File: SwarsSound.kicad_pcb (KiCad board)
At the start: 2 copper layers, 292.1 x 227.3 mm, 168 parts, among them P1 Main_Connector, P2 aud_con, P3 edge_con, Q1 2N3906f, Q2 2N3906f, Q3 2N3904, Q4 2N3904

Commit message: more traces
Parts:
- moved R27 2.62 mm to (117.5, 111.1), turned to 270 degrees
- moved C28 1.27 mm to (132.1, 172.7), turned to 0 degrees
- turned R26 to 0 degrees
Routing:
- net SPEECH: track 3.81 -> 171.4 mm
- net Net-(D-2-Pad24): track 0.00 -> 123.0 mm, vias 0 -> 1
- net +5A: track 0.00 -> 73.2 mm
- net Net-(C40-Pad1): track 0.00 -> 41.3 mm
- net CO3: track 28.4 -> 0.00 mm
- net CO2: track 14.6 -> 33.6 mm
- net Net-(C38-Pad1): track 0.00 -> 14.5 mm
- net Net-(C-4-Pad7): track 0.00 -> 11.0 mm
- net Net-(C42-Pad1): track 0.00 -> 10.8 mm
- net Net-(C56-Pad1): track 5.08 -> 9.12 mm

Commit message: more traces
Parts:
- moved R8 1.27 mm to (132.7, 35.6), turned to 90 degrees
- moved R9 1.27 mm to (132.7, 38.1), turned to 90 degrees
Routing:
- net SD4: track 266.2 -> 334.3 mm, vias 3 -> 4
- net SD3: track 271.8 -> 339.8 mm, vias 2 -> 3
- net SD6: track 283.9 -> 349.2 mm, vias 3 -> 4
- net SD5: track 277.1 -> 342.0 mm, vias 3 -> 5
- net SD2: track 260.9 -> 319.4 mm, vias 3 -> 4
- net SD7: track 287.2 -> 340.8 mm, vias 3 -> 5
- net SD1: track 257.0 -> 310.5 mm, vias 4 -> 5
- net SA0: track 289.8 -> 342.4 mm, vias 2 -> 4
- net SD0: track 253.4 -> 301.5 mm, vias 2 -> 3
- net DXMT: track 0.00 -> 43.1 mm
- net SA2: track 286.3 -> 327.0 mm, vias 3 -> 5
- net DRCV: track 0.00 -> 38.3 mm
- net CO3: track 0.00 -> 28.7 mm
- net SA5: track 261.7 -> 287.6 mm
- net SA1: track 289.2 -> 307.8 mm, vias 2 -> 3

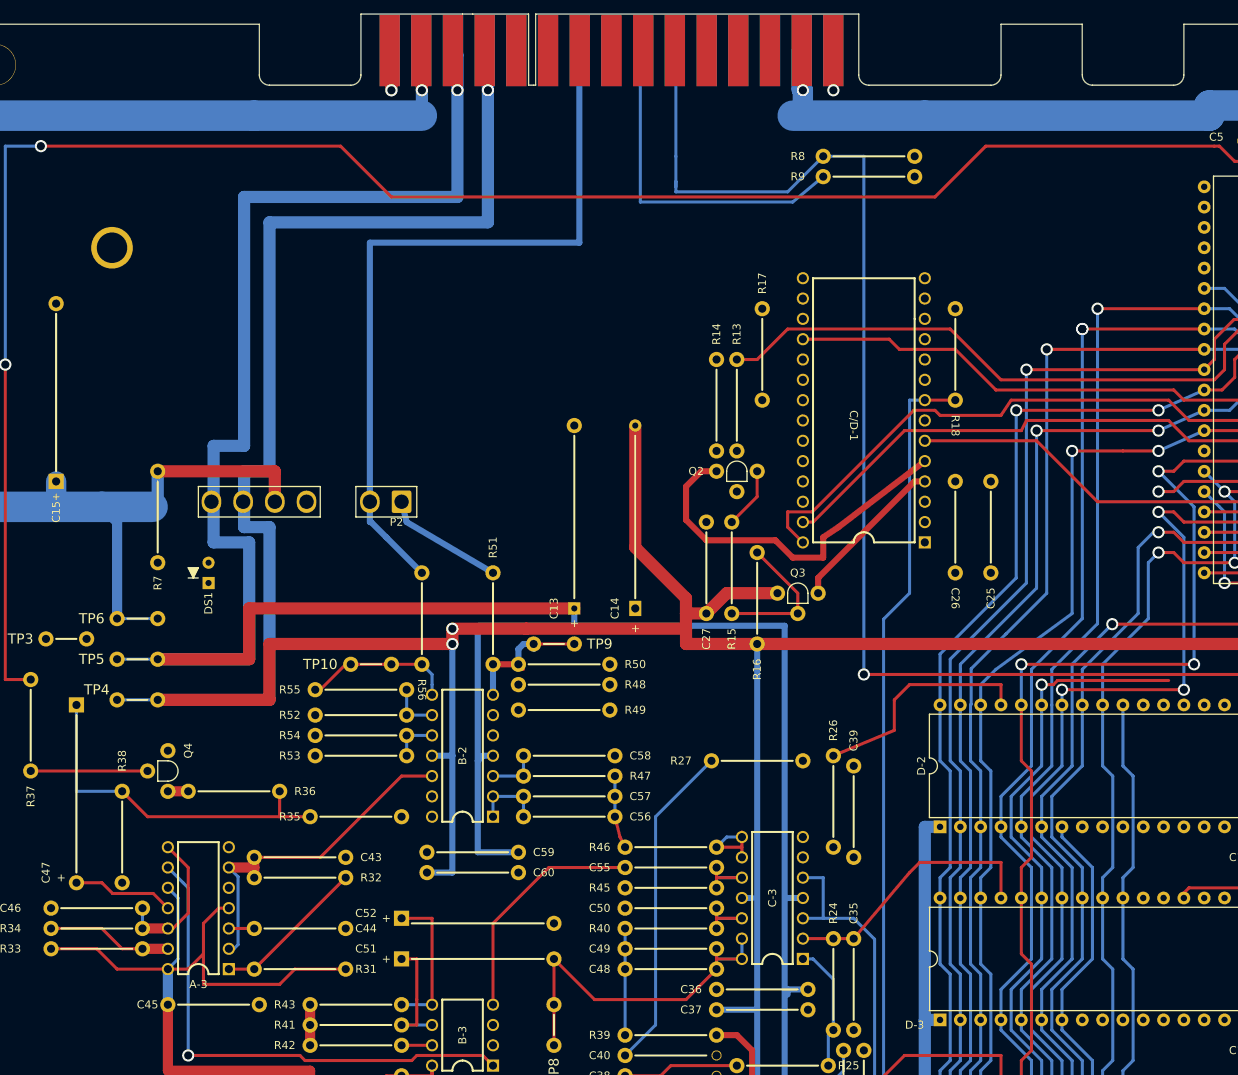
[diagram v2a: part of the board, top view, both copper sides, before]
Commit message: Modified some traces
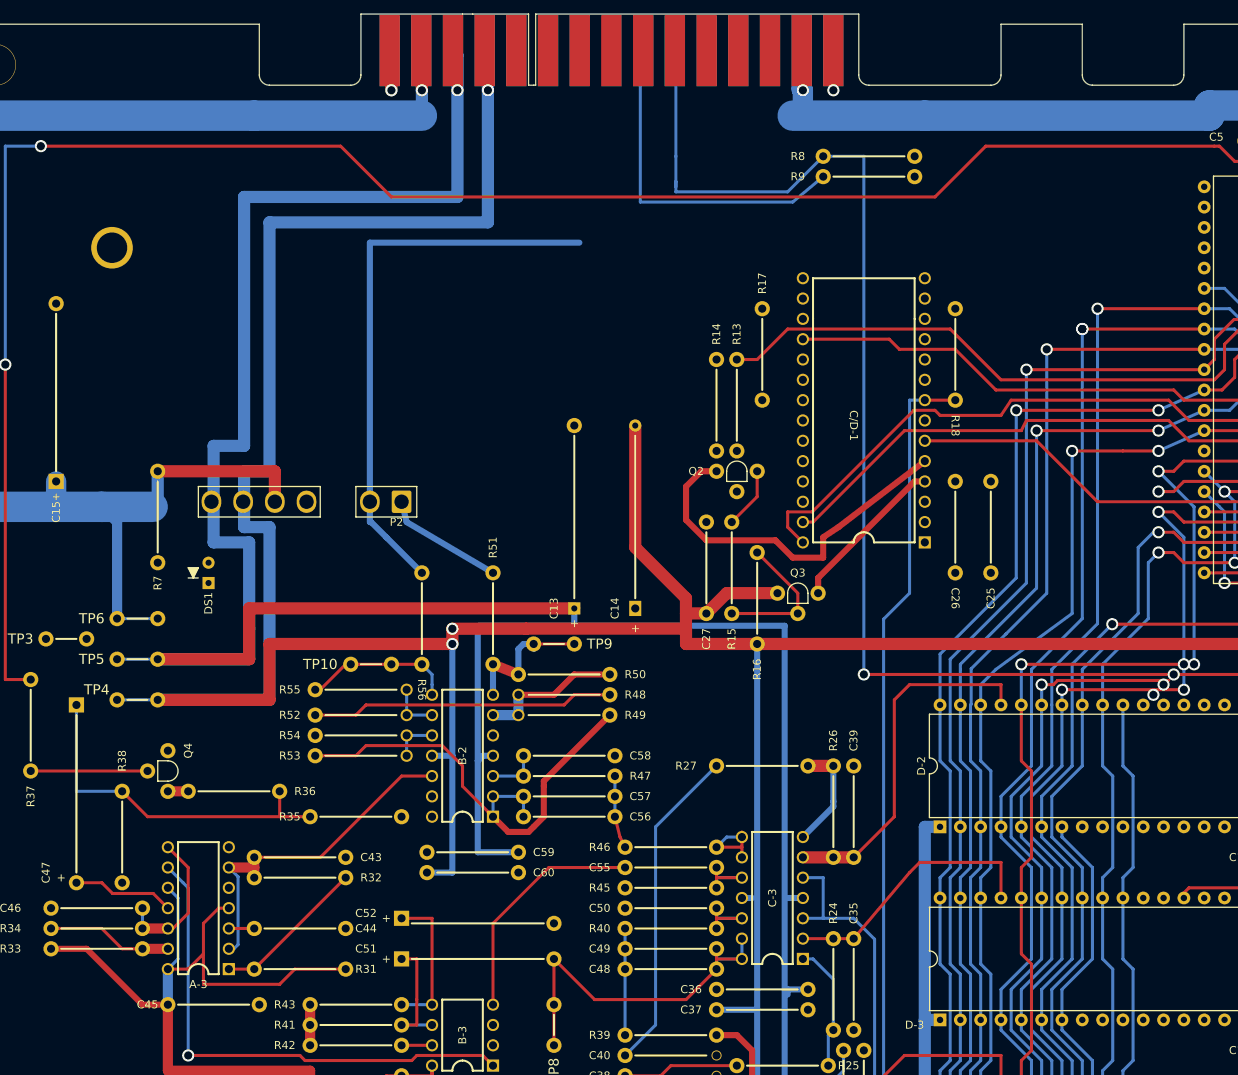
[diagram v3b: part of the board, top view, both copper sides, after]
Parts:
- moved R49 3.81 mm to (93.3, 105.4)
- moved R48 1.91 mm to (93.3, 102.9)
- moved R50 1.27 mm to (93.3, 100.3)
- moved R27 0.90 mm to (118.1, 111.8)
- turned R26 to 180 degrees
- renumbered R49 to R48, R48 to R49
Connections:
- P3 pad F: RT_AUD -> LT_AUD
- P3 pad H: LT_AUD -> RT_AUD
- R52 pad 2: Net-(B-2-Pad1) -> AUD
- R53 pad 2: AUD -> Net-(B-2-Pad1)
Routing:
- net Net-(B-2-Pad1): track 8.89 -> 60.9 mm
- net AUD: track 48.8 -> 86.6 mm
- net LT_AUD: track 94.7 -> 70.7 mm
- net Net-(B-2-Pad6): track 0.00 -> 18.2 mm
- net CO3: track 28.7 -> 44.8 mm
- net Net-(C-3-Pad7): track 0.00 -> 13.6 mm
- net +12V: track 482.7 -> 484.6 mm
- net Net-(B-2-Pad7): track 17.4 -> 18.3 mm
- net (no net): vias 0 -> 4

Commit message: more traces
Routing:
- net RT_AUD: track 15.2 -> 93.5 mm
- net LT_AUD: track 70.7 -> 91.0 mm

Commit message: more traces
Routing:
- net Net-(E-1-Pad12): track 0.00 -> 43.2 mm, vias 0 -> 2
- net +5V: track 1489.4 -> 1525.0 mm
- net S~IRQ: track 0.00 -> 19.6 mm

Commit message: more traces
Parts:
- moved C8 1.27 mm to (252.7, 191.8)
- moved C20 0.63 mm to (254.6, 151.1)
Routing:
- net PD6: track 12.4 -> 236.8 mm, vias 1 -> 2
- net PD7: track 11.2 -> 225.6 mm, vias 1 -> 2
- net PD5: track 13.7 -> 223.0 mm, vias 1 -> 2
- net PD4: track 15.6 -> 218.6 mm, vias 1 -> 2
- net PD2: track 17.5 -> 212.0 mm, vias 1 -> 2
- net PD3: track 16.3 -> 200.8 mm, vias 1 -> 2
- net PD1: track 18.8 -> 198.3 mm, vias 1 -> 2
- net +5V: track 1525.0 -> 1701.3 mm
- net ~SOUND: track 25.6 -> 199.7 mm
- net PD0: track 20.7 -> 193.2 mm, vias 1 -> 2
- net AB0: track 23.9 -> 163.6 mm
- net R/~WB: track 25.1 -> 146.9 mm
- net SD0: track 301.5 -> 406.8 mm, vias 3 -> 6
- net SD2: track 319.4 -> 422.6 mm, vias 4 -> 5
- net SD4: track 334.3 -> 435.4 mm, vias 4 -> 7
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
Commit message: Even more traces
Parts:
- moved C12 0.63 mm to (290.8, 192.4)
- moved C8 0.63 mm to (252.7, 192.4)
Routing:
- net ɸE: track 191.8 -> 302.6 mm
- net ~MAINREAD: track 42.0 -> 124.6 mm, vias 1 -> 2
- net ~FLAGREAD: track 0.00 -> 75.6 mm, vias 0 -> 1
- net ~SOUNDWR: track 0.00 -> 61.7 mm, vias 0 -> 2
- net ~MAINWR: track 0.00 -> 47.7 mm, vias 0 -> 1
- net Net-(H-2-Pad2): track 0.00 -> 28.0 mm
- net CLKQ: track 168.5 -> 195.5 mm
- net PD6: track 236.8 -> 263.3 mm
- net SOUNDFLAG: track 0.00 -> 9.94 mm
- net ~SRES: track 0.00 -> 8.67 mm
- net +5V: track 1701.3 -> 1703.2 mm
- net SD0: track 406.8 -> 407.7 mm
- net GND: track 173.5 -> 172.9 mm
- net (no net): vias 4 -> 0

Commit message: more traces
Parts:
- moved C7 2.54 mm to (255.3, 125.7), turned to 90 degrees
- turned C10 to 270 degrees
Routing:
- net +5V: track 1703.2 -> 1931.5 mm
- net ~SRES: track 8.67 -> 162.9 mm, vias 0 -> 3
- net SR\~W: track 150.8 -> 272.6 mm, vias 4 -> 6
- net (no net): track 0.00 -> 108.5 mm
- net Net-(F/H-1-Pad20): track 0.00 -> 92.6 mm
- net Net-(F-5-Pad10): track 2.54 -> 84.4 mm, vias 0 -> 1
- net Net-(F-3-Pad15): track 0.00 -> 53.8 mm, vias 0 -> 2
- net Net-(F-3-Pad9): track 0.00 -> 41.8 mm, vias 0 -> 2
- net SA12: track 58.0 -> 93.8 mm
- net SA11: track 87.0 -> 122.8 mm
- net SA13: track 0.00 -> 26.4 mm, vias 0 -> 1
- net SA14: track 0.00 -> 24.3 mm
- net Net-(H-2-Pad1): track 0.00 -> 19.7 mm
- net Net-(Q1-Pad2): track 0.00 -> 15.9 mm
- net Net-(F-3-Pad12): track 0.00 -> 5.08 mm
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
